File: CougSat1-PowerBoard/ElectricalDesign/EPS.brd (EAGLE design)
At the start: 90.4 x 95.8 mm, 428 parts, among them J1 Deployable 0, J10 Battery -, J11 PGND, J12 Battery +, J13 VBatt, J2 PV0, J3 PV1, J4 Umbilical, J5 CougSat Card, J6 SWD, J7 PV2, J8 PV3, J9 Deployable 1, Q1 CSD25402Q3A, Q10 CSD25402Q3A, Q11 DMN53D0LDW, Q12 CSD25402Q3A, Q13 DMN53D0LDW, Q14 CSD25402Q3A, Q15 DMN53D0LDW, Q16 CSD25402Q3A, Q17 CSD25402Q3A, Q18 CSD25402Q3A, Q19 DMN53D0LDW, Q2 DMN2008LFU, Q20 CSD25402Q3A, Q21 CSD25402Q3A, Q22 CSD25402Q3A, Q23 DMN53D0LDW, Q24 CSD25402Q3A, Q25 DMN53D0LDW, Q26 CSD25402Q3A, Q27 DMN53D0LDW, Q28 CSD25402Q3A, Q29 CSD25402Q3A, Q3 DMN2008LFU, Q30 CSD25402Q3A, Q31 DMN53D0LDW, Q32 CSD25402Q3A, Q33 DMN53D0LDW, Q34 CSD25402Q3A, Q35 CSD25402Q3A, Q36 DMN53D0LDW, Q37 CSD25402Q3A, Q38 CSD25402Q3A, Q39 DMN53D0LDW, Q4 CSD25402Q3A, Q40 CSD25402Q3A, Q41 CSD25402Q3A, Q42 DMN53D0LDW, Q43 CSD25402Q3A, Q5 DMN53D0LDW, Q6 DMN53D0LDW, Q7 CSD25402Q3A, Q8 CSD25402Q3A, Q9 CSD25402Q3A, SW1 ESE24MH1, U1 INA199C2, U10 INA199C2, U11 INA199C1, U12 AD7689, U13 INA199C2, U14 INA199C2, U15 TXS0102DQM, U16 TXS0102DQM, U17 AD8515, U18 BQ29700, U19 INA199C2, U2 AD7689, U20 TXS0102DQM, U21 TXS0102DQM, U22 STM32L476RGT, U23 AD7291, U24 INA199C2, U25 INA199C2, U26 BQ29700, U27 INA199C2, U28 INA199C2, U29 INA199C2, U3 AD8515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

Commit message: Adjusted notes
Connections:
- new net CHASSIS_RBF0: C55.1, H4.1, H4.V1, H4.V2, H4.V3, H4.V4, H4.V5, H4.V6, H4.V7, H4.V8, R34.2
- new net CHASSIS_RBF1: C77.1, H3.1, H3.V1, H3.V2, H3.V3, H3.V4, H3.V5, H3.V6, H3.V7, H3.V8, R48.2
- net CHASSIS: no longer C55.1, C77.1, H3.1, H3.V1, H3.V2, H3.V3, H3.V4, H3.V5, H3.V6, H3.V7, H3.V8, H4.1, H4.V1, H4.V2, H4.V3, H4.V4, H4.V5, H4.V6, H4.V7, H4.V8, R34.2, R48.2
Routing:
- net CHASSIS: track 310.6 -> 252.5 mm
- net CHASSIS_RBF1: track 0.00 -> 36.2 mm
- net CHASSIS_RBF0: track 0.00 -> 17.7 mm
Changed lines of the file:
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@@
 </signal>
 <signal name="CHASSIS" class="1">
-<contactref element="H3" pad="1"/>
-<contactref element="H3" pad="V1"/>
-<contactref element="H3" pad="V2"/>
-<contactref element="H3" pad="V3"/>
-<contactref element="H3" pad="V4"/>
-<contactref element="H3" pad="V5"/>
-<contactref element="H3" pad="V6"/>
-<contactref element="H3" pad="V7"/>
-<contactref element="H3" pad="V8"/>
-<contactref element="C77" pad="1"/>
-<contactref element="R48" pad="2"/>
-<contactref element="H4" pad="1"/>
-<contactref element="H4" pad="V1"/>
-<contactref element="H4" pad="V2"/>
-<contactref element="H4" pad="V3"/>
-<contactref element="H4" pad="V4"/>
-<contactref element="H4" pad="V5"/>
-<contactref element="H4" pad="V6"/>
-<contactref element="H4" pad="V7"/>
-<contactref element="H4" pad="V8"/>
-<contactref element="C55" pad="1"/>
-<contactref element="R34" pad="2"/>
 <contactref element="J5" pad="CHASSIS@1"/>
 <contactref element="J5" pad="CHASSIS@2"/>
 <contactref element="J5" pad="CHASSIS@3"/>
 <contactref element="J5" pad="CHASSIS@4"/>
-<wire x1="75.9" y1="5.5" x2="77.031371875" y2="6.631371875" width="0.2" layer="16"/>
-<wire x1="75.9" y1="5.5" x2="75.9" y2="7.1" width="0.2" layer="16"/>
-<wire x1="75.9" y1="5.5" x2="74.768628125" y2="6.631371875" width="0.2" layer="16"/>
-<wire x1="75.9" y1="5.5" x2="74.3" y2="5.5" width="0.2" layer="16"/>
-<wire x1="75.9" y1="5.5" x2="74.768628125" y2="4.368628125" width="0.2" layer="16"/>
-<wire x1="75.9" y1="5.5" x2="75.9" y2="3.9" width="0.2" layer="16"/>
-<wire x1="75.9" y1="5.5" x2="77.031371875" y2="4.368628125" width="0.2" layer="16"/>
-<wire x1="75.9" y1="5.5" x2="77.5" y2="5.5" width="0.2" layer="16"/>
-<wire x1="84.25" y1="-6.6" x2="84.25" y2="-5.5" width="0.2" layer="16"/>
-<wire x1="84.25" y1="-5.5" x2="84.25" y2="-4.9" width="0.2" layer="16"/>
-<wire x1="87.4" y1="-5.5" x2="85.8" y2="-5.5" width="0.2" layer="16"/>
-<wire x1="87.4" y1="-5.5" x2="86.268628125" y2="-4.368628125" width="0.2" layer="16"/>
-<wire x1="87.4" y1="-5.5" x2="87.4" y2="-3.9" width="0.2" layer="16"/>
-<wire x1="87.4" y1="-5.5" x2="88.531371875" y2="-4.368628125" width="0.2" layer="16"/>
-<wire x1="87.4" y1="-5.5" x2="89" y2="-5.5" width="0.2" layer="16"/>
-<wire x1="87.4" y1="-5.5" x2="88.531371875" y2="-6.631371875" width="0.2" layer="16"/>
-<wire x1="87.4" y1="-5.5" x2="87.4" y2="-7.1" width="0.2" layer="16"/>
-<wire x1="87.4" y1="-5.5" x2="86.268628125" y2="-6.631371875" width="0.2" layer="16"/>
-<wire x1="87.4" y1="-5.5" x2="84.25" y2="-5.5" width="0.2" layer="16"/>
-<wire x1="75.9" y1="5.5" x2="75.9" y2="8.55" width="0.2" layer="16"/>
-<wire x1="75.9" y1="8.55" x2="76.15" y2="8.8" width="0.2" layer="16"/>
-<wire x1="79.2" y1="7.65" x2="78.05" y2="7.65" width="0.2" layer="16"/>
-<wire x1="78.05" y1="7.65" x2="77.031371875" y2="6.631371875" width="0.2" layer="16"/>
 <wire x1="50.2" y1="46.1" x2="57.3" y2="46.1" width="0.2" layer="16"/>
 <wire x1="50.2" y1="46.1" x2="57.3" y2="46.1" width="0.2" layer="1"/>
 <wire x1="46.2" y1="-46.1" x2="57.3" y2="-46.1" width="0.2" layer="1"/>
 <wire x1="46.2" y1="-46.1" x2="57.3" y2="-46.1" width="0.2" layer="16"/>
-<wire x1="88.531371875" y1="-6.631371875" x2="90" y2="-8.1" width="0.2" layer="16"/>
 <wire x1="90" y1="-46.1" x2="57.3" y2="-46.1" width="0.2" layer="16"/>
 <wire x1="90" y1="-8.1" x2="90" y2="-46.1" width="0.2" layer="16"/>
-<wire x1="84.25" y1="-4.9" x2="84.25" y2="-3.95" width="0.2" layer="16"/>
-<wire x1="84.25" y1="-3.95" x2="83.7" y2="-3.4" width="0.2" layer="16"/>
-<wire x1="83.7" y1="-3.4" x2="75.32" y2="-3.4" width="0.2" layer="16"/>
-<wire x1="75.32" y1="-3.4" x2="74.5" y2="-2.58" width="0.2" layer="16"/>
-<wire x1="75.82" y1="3.9" x2="75.9" y2="3.9" width="0.2" layer="16"/>
-<wire x1="74.5" y1="-2.58" x2="74.5" y2="2.58" width="0.2" layer="16"/>
-<wire x1="74.5" y1="2.58" x2="75.82" y2="3.9" width="0.2" layer="16"/>
 <wire x1="38.91" y1="38.06" x2="38.76" y2="38.21" width="0.2" layer="16"/>
 <wire x1="38.91" y1="31.11" x2="38.91" y2="38.06" width="0.2" layer="16"/>
@@
 <wire x1="37.2" y1="-31.51" x2="37.4" y2="-31.31" width="0.2" layer="1"/>
 <wire x1="37.3" y1="-46.1" x2="37.3" y2="-36.6" width="0.2" layer="1"/>
-<wire x1="77.86" y1="7.46" x2="77.031371875" y2="6.631371875" width="0.2" layer="1"/>
 <wire x1="85.48" y1="7.46" x2="77.86" y2="7.46" width="0.2" layer="1"/>
 <polygon width="0.2" layer="1" thermals="no" rank="6">
@@
 </polygon>
 <wire x1="50.2" y1="46.1" x2="50.2" y2="46.1" width="0" layer="19" extent="1-16"/>
+<wire x1="90" y1="-8.1" x2="77.86" y2="7.46" width="0" layer="19" extent="1-16"/>
 <wire x1="46.2" y1="-46.1" x2="46.2" y2="-46.1" width="0" layer="19" extent="1-16"/>
 </signal>
@@
 <wire x1="4.45" y1="-43.85" x2="-13.25" y2="-198.25" width="0" layer="19" extent="1-16"/>
 </signal>
+<signal name="CHASSIS_RBF0" class="1">
+<contactref element="H4" pad="1"/>
+<contactref element="H4" pad="V1"/>
+<contactref element="H4" pad="V2"/>
+<contactref element="H4" pad="V3"/>
+<contactref element="H4" pad="V4"/>
+<contactref element="H4" pad="V5"/>
+<contactref element="H4" pad="V6"/>
+<contactref element="H4" pad="V7"/>
+<contactref element="H4" pad="V8"/>
+<contactref element="C55" pad="1"/>
+<contactref element="R34" pad="2"/>
+<wire x1="84.25" y1="-6.6" x2="84.25" y2="-5.5" width="0.2" layer="16"/>
+<wire x1="84.25" y1="-5.5" x2="84.25" y2="-4.9" width="0.2" layer="16"/>
+<wire x1="87.4" y1="-5.5" x2="85.8" y2="-5.5" width="0.2" layer="16"/>
+<wire x1="87.4" y1="-5.5" x2="86.268628125" y2="-4.368628125" width="0.2" layer="16"/>
+<wire x1="87.4" y1="-5.5" x2="87.4" y2="-3.9" width="0.2" layer="16"/>
+<wire x1="87.4" y1="-5.5" x2="88.531371875" y2="-4.368628125" width="0.2" layer="16"/>
+<wire x1="87.4" y1="-5.5" x2="89" y2="-5.5" width="0.2" layer="16"/>
+<wire x1="87.4" y1="-5.5" x2="88.531371875" y2="-6.631371875" width="0.2" layer="16"/>
+<wire x1="87.4" y1="-5.5" x2="87.4" y2="-7.1" width="0.2" layer="16"/>
+<wire x1="87.4" y1="-5.5" x2="86.268628125" y2="-6.631371875" width="0.2" layer="16"/>
+<wire x1="87.4" y1="-5.5" x2="84.25" y2="-5.5" width="0.2" layer="16"/>
+</signal>
+<signal name="CHASSIS_RBF1" class="1">
+<contactref element="H3" pad="1"/>
+<contactref element="H3" pad="V1"/>
+<contactref element="H3" pad="V2"/>
+<contactref element="H3" pad="V3"/>
+<contactref element="H3" pad="V4"/>
+<contactref element="H3" pad="V5"/>
+<contactref element="H3" pad="V6"/>
+<contactref element="H3" pad="V7"/>
+<contactref element="H3" pad="V8"/>
+<contactref element="C77" pad="1"/>
+<contactref element="R48" pad="2"/>
+<wire x1="75.9" y1="5.5" x2="77.031371875" y2="6.631371875" width="0.2" layer="16"/>
+<wire x1="75.9" y1="5.5" x2="75.9" y2="7.1" width="0.2" layer="16"/>
+<wire x1="75.9" y1="5.5" x2="74.768628125" y2="6.631371875" width="0.2" layer="16"/>
+<wire x1="75.9" y1="5.5" x2="74.3" y2="5.5" width="0.2" layer="16"/>
+<wire x1="75.9" y1="5.5" x2="74.768628125" y2="4.368628125" width="0.2" layer="16"/>
+<wire x1="75.9" y1="5.5" x2="75.9" y2="3.9" width="0.2" layer="16"/>
+<wire x1="75.9" y1="5.5" x2="77.031371875" y2="4.368628125" width="0.2" layer="16"/>
+<wire x1="75.9" y1="5.5" x2="77.5" y2="5.5" width="0.2" layer="16"/>
+<wire x1="75.9" y1="5.5" x2="75.9" y2="8.55" width="0.2" layer="16"/>
+<wire x1="75.9" y1="8.55" x2="76.15" y2="8.8" width="0.2" layer="16"/>
+<wire x1="79.2" y1="7.65" x2="78.05" y2="7.65" width="0.2" layer="16"/>
+<wire x1="78.05" y1="7.65" x2="77.031371875" y2="6.631371875" width="0.2" layer="16"/>
+<wire x1="84.25" y1="-3.95" x2="83.7" y2="-3.4" width="0.2" layer="16"/>
+<wire x1="83.7" y1="-3.4" x2="75.32" y2="-3.4" width="0.2" layer="16"/>
+<wire x1="75.32" y1="-3.4" x2="74.5" y2="-2.58" width="0.2" layer="16"/>
+<wire x1="75.82" y1="3.9" x2="75.9" y2="3.9" width="0.2" layer="16"/>
+<wire x1="74.5" y1="-2.58" x2="74.5" y2="2.58" width="0.2" layer="16"/>
+<wire x1="74.5" y1="2.58" x2="75.82" y2="3.9" width="0.2" layer="16"/>
+</signal>
 </signals>

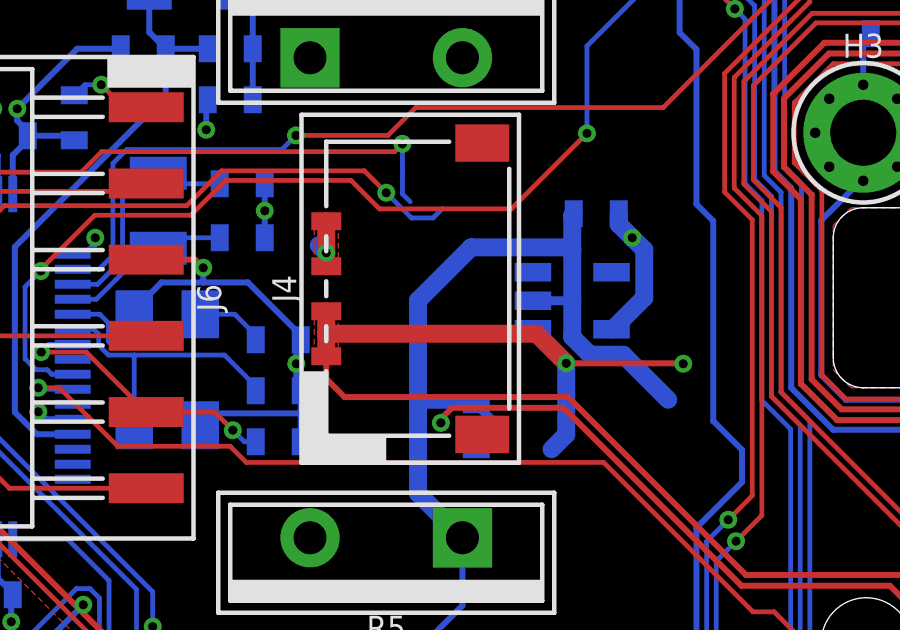
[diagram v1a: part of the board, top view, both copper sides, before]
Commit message: Added power inhibit page
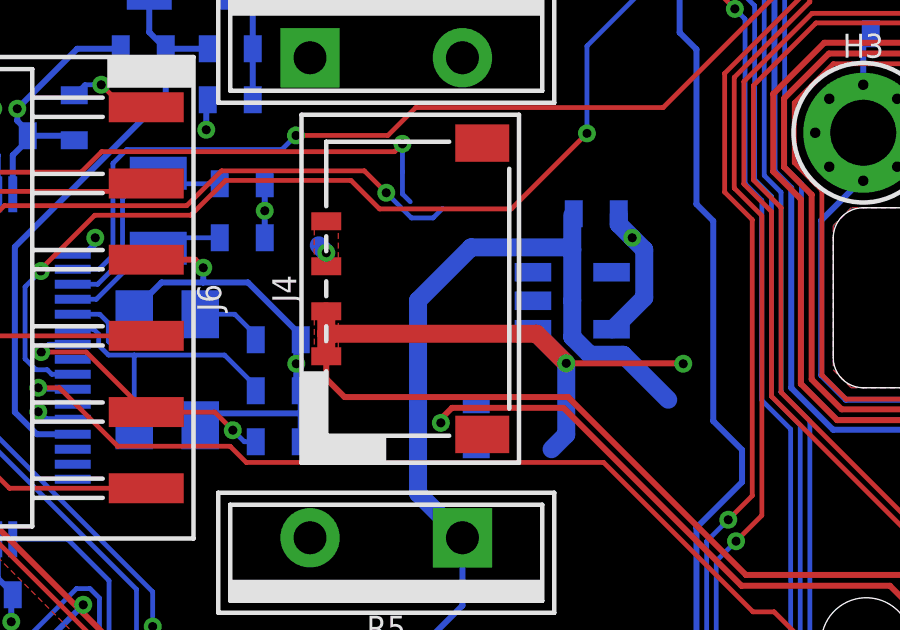
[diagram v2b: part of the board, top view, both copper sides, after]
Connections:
- net BATTERY-: now also C61.2, C67.2, D11.2, J4.3, J4.4
- net PGND: no longer C61.2, C67.2, D11.2, J4.3, J4.4
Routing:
- net PGND: track 832.2 -> 826.7 mm
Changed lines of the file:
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@@
 <contactref element="J2" pad="7"/>
 <contactref element="J2" pad="6"/>
-<contactref element="J4" pad="3"/>
-<contactref element="J4" pad="4"/>
 <contactref element="J1" pad="4"/>
 <contactref element="D20" pad="2"/>
@@
 <contactref element="D1" pad="2"/>
 <contactref element="D3" pad="2"/>
-<contactref element="D11" pad="2"/>
 <contactref element="C123" pad="2"/>
 <contactref element="C128" pad="2"/>
@@
 <contactref element="C117" pad="2"/>
 <contactref element="C6" pad="2"/>
-<contactref element="C61" pad="2"/>
-<contactref element="C67" pad="2"/>
 <contactref element="J9" pad="4"/>
 <contactref element="R4" pad="1"/>
@@
 <wire x1="44.9" y1="20.8" x2="45.6" y2="20.1" width="0.6" layer="2"/>
 <wire x1="44.9" y1="23.2" x2="44.9" y2="20.8" width="0.6" layer="2"/>
-<wire x1="58" y1="1.05" x2="58" y2="1.5" width="0.6" layer="1"/>
-<wire x1="58" y1="1.5" x2="58" y2="2.55" width="0.6" layer="1"/>
 <via x="58" y="1.5" extent="1-16" drill="0.3"/>
 <wire x1="58" y1="1.5" x2="57.75" y2="1.75" width="0.6" layer="16"/>
@@
 <wire x1="66.79" y1="-1.9" x2="66.2" y2="-1.31" width="0.6" layer="16"/>
 <wire x1="66.2" y1="-1.31" x2="66.2" y2="-0.1" width="0.6" layer="16"/>
-<wire x1="64.89" y1="-0.1" x2="66.2" y2="-0.1" width="0.3" layer="16"/>
-<wire x1="63" y1="-3.55" x2="63.55" y2="-4.1" width="0.3" layer="16"/>
 <wire x1="62.54" y1="-8" x2="61.06" y2="-6.52" width="0.6" layer="16"/>
 <wire x1="61.06" y1="-6.52" x2="61.06" y2="-3.5" width="0.6" layer="16"/>
 <wire x1="61.06" y1="-3.5" x2="61.06" y2="-0.09" width="0.6" layer="16"/>
 <wire x1="61.06" y1="-0.09" x2="62.83" y2="1.68" width="0.6" layer="16"/>
-<wire x1="66.2" y1="2.75" x2="66.25" y2="2.8" width="0.6" layer="16"/>
 <wire x1="66.2" y1="-0.1" x2="66.2" y2="1.6" width="0.6" layer="16"/>
 <wire x1="66.2" y1="1.6" x2="66.2" y2="2.75" width="0.6" layer="16"/>
 <wire x1="62.83" y1="1.68" x2="66.12" y2="1.68" width="0.6" layer="16"/>
 <wire x1="66.12" y1="1.68" x2="66.2" y2="1.6" width="0.6" layer="16"/>
-<wire x1="63" y1="-3.55" x2="61.11" y2="-3.55" width="0.3" layer="16"/>
 <wire x1="61.11" y1="-3.55" x2="61.06" y2="-3.5" width="0.3" layer="16"/>
 <wire x1="84.3" y1="35" x2="77.7" y2="35" width="0.2" layer="2"/>
@@
 <wire x1="66.6" y1="37.05" x2="68.05" y2="36.7" width="0" layer="19" extent="16-16"/>
 <wire x1="73.65" y1="36.7" x2="71" y2="36.7" width="0" layer="19" extent="16-16"/>
-<wire x1="58" y1="2.55" x2="57.75" y2="7.71" width="0" layer="19" extent="1-16"/>
 <wire x1="6.1" y1="5.5" x2="11.8" y2="5.7" width="0" layer="19" extent="1-2"/>
+<wire x1="57.75" y1="1.75" x2="57.75" y2="7.71" width="0" layer="19" extent="16-16"/>
 </signal>
 <signal name="PV_I2C_SDA">
@@
 <wire x1="13.8" y1="-5.4" x2="13.8" y2="-9.615" width="0.5" layer="1"/>
 <contactref element="J10" pad="1"/>
-<wire x1="12.8" y1="-10.8" x2="-9.7" y2="-48.5" width="0" layer="19" extent="1-1"/>
+<contactref element="D11" pad="2"/>
+<contactref element="J4" pad="3"/>
+<contactref element="J4" pad="4"/>
+<contactref element="C67" pad="2"/>
+<contactref element="C61" pad="2"/>
+<wire x1="64.89" y1="-0.1" x2="66.25" y2="2.8" width="0" layer="19" extent="16-16"/>
+<wire x1="63" y1="-3.55" x2="64.89" y2="-0.1" width="0" layer="19" extent="16-16"/>
+<wire x1="58" y1="1.05" x2="63" y2="-3.55" width="0" layer="19" extent="1-16"/>
+<wire x1="58" y1="2.55" x2="58" y2="1.05" width="0" layer="19" extent="1-1"/>
+<wire x1="16.2" y1="-8.85" x2="58" y2="1.05" width="0" layer="19" extent="1-16"/>
 <wire x1="8.5" y1="6.35" x2="12.3" y2="-3.9" width="0" layer="19" extent="16-16"/>
 <wire x1="7.9" y1="9.6" x2="9.45" y2="7.9" width="0" layer="19" extent="16-16"/>
+<wire x1="-9.7" y1="-48.5" x2="12.8" y2="-10.8" width="0" layer="19" extent="1-1"/>
 </signal>
 <signal name="VBATT">
